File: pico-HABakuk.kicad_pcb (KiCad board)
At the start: 2 copper layers, 52 x 51 mm, 34 parts, among them J1 USB_B_Micro, J2 Conn_01x02, J3 Conn_02x18_Odd_Even, J4 Conn_02x18_Odd_Even, U1 NCP1117-3.3_SOT223, U2 W25Q128JVS, U3 RP2040, Y1 ABM8-272-T3

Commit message: First changes in the sch and pcb
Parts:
- removed J3, J4: Conn_02x18_Odd_Even, Connector_PinHeader_2.54mm:PinHeader_2x18_P2.54mm_Vertical
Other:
- board text added: "RP2040"
- board text added: "pico-HABakuk"
- board text removed: "Minimal Design Example REV2"
- board text removed: "Outer Row GND"
- board text removed: "Raspberry Pi RP2040"

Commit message: More work on schematics
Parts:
- removed H1, H2, H3, H4: MountingHole, MountingHole:MountingHole_2.7mm_M2.5
- removed R2: DNF, Resistor_SMD:R_0402_1005Metric
- added C18: 10u/4, Capacitor_SMD:C_0603_1608Metric, F.Cu at (137.7, 90.8)
- added C19: 10u/4, Capacitor_SMD:C_0603_1608Metric, F.Cu at (137.7, 93.3)
- added C20: 10u/4, Capacitor_SMD:C_0603_1608Metric, F.Cu at (137.7, 95.8)
- added C21: 1n, Capacitor_SMD:C_0603_1608Metric, F.Cu at (137.7, 98.3)
- added C22: 1u, Capacitor_SMD:C_0603_1608Metric, F.Cu at (141.7, 90.8)
- added C23: 1n, Capacitor_SMD:C_0603_1608Metric, F.Cu at (141.7, 93.3)
- added C24: 10u/10, Capacitor_SMD:C_0805_2012Metric, F.Cu at (149.9, 94.6)
- added D2: WS2812B-2020, LED_SMD:LED_WS2812B-2020_PLCC4_2.0x2.0mm, F.Cu at (154.1, 91.3)
- added J4: Ant-, Connector_PinHeader_2.54mm:PinHeader_1x01_P2.54mm_Vertical, F.Cu at (160.8, 109.6)
- added J5: Solar, Connector_PinSocket_2.54mm:PinSocket_1x02_P2.54mm_Vertical, F.Cu at (148.0, 101.9)
- added J7: Ultra_Cap, Connector_PinSocket_2.54mm:PinSocket_1x02_P2.54mm_Vertical, F.Cu at (152.6, 101.9)
- added JP1: Solar_voltage, Jumper:SolderJumper-2_P1.3mm_Bridged_RoundedPad1.0x1.5mm, F.Cu at (149.9, 91.3)
- added L1: 10u, Inductor_SMD:L_Taiyo-Yuden_MD-3030, F.Cu at (149.6, 115.4)
- added R10: 360k, Resistor_SMD:R_0603_1608Metric, F.Cu at (145.7, 95.8)
- added R11: 220k, Resistor_SMD:R_0603_1608Metric, F.Cu at (145.7, 98.3)
- added R6: 1k, Resistor_SMD:R_0603_1608Metric, F.Cu at (141.7, 95.8)
- added R7: 1k, Resistor_SMD:R_0603_1608Metric, F.Cu at (141.7, 98.3)
- added R8: 1k, Resistor_SMD:R_0603_1608Metric, F.Cu at (145.7, 90.8)
- added R9: 510m, Resistor_SMD:R_0603_1608Metric, F.Cu at (145.7, 93.3)
- added SW1: USB BOOT, Button_Switch_SMD:SW_SPST_Omron_B3FS-100xP, F.Cu at (138.7, 119.0)
- added SW2: RESET, Button_Switch_SMD:SW_SPST_Omron_B3FS-100xP, F.Cu at (138.9, 107.5)
- added TP1: +3V3, Connector_Pin:Pin_D1.1mm_L8.5mm_W2.5mm_FlatFork, F.Cu at (137.9, 83.1)
- added TP2: USB_D+, Connector_Pin:Pin_D1.1mm_L8.5mm_W2.5mm_FlatFork, F.Cu at (137.9, 87.4)
- added TP3: USB_D-, Connector_Pin:Pin_D1.1mm_L8.5mm_W2.5mm_FlatFork, F.Cu at (142.5, 83.1)
- added TP4: GND, Connector_Pin:Pin_D1.1mm_L8.5mm_W2.5mm_FlatFork, F.Cu at (142.5, 87.4)
- added TP5: USB_BOOT, Connector_Pin:Pin_D1.1mm_L8.5mm_W2.5mm_FlatFork, F.Cu at (147.0, 83.1)
- added TP6: Reset, Connector_Pin:Pin_D1.1mm_L8.5mm_W2.5mm_FlatFork, F.Cu at (147.0, 87.4)
- added TP7: SWCLK, Connector_Pin:Pin_D1.1mm_L8.5mm_W2.5mm_FlatFork, F.Cu at (151.6, 83.1)
- added TP8: SWD, Connector_Pin:Pin_D1.1mm_L8.5mm_W2.5mm_FlatFork, F.Cu at (151.6, 87.4)
- added U4: SPV1040T, Package_SO:TSSOP-8_4.4x3mm_P0.65mm, F.Cu at (150.1, 109.0)
- added U5: LM4040DBZ-3, Package_TO_SOT_SMD:SOT-23, F.Cu at (149.4, 126.1)
- C10: value 1u -> 2u2
- J2: value Conn_01x02 -> Ant+; footprint Connector_PinHeader_2.54mm:PinHeader_1x02_P2.54mm_Vertical -> Connector_PinHeader_2.54mm:PinHeader_1x01_P2.54mm_Vertical
- moved J2 74.0 mm to (160.8, 101.4), turned to 0 degrees
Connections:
- net /XIN renamed Net-(U3-XIN)
- net /XOUT renamed Net-(U3-XOUT)
- net VBUS renamed Net-(J1-VBUS)
- C10 pad 1: +3V3 -> Net-(U3-VREG_IN)
- J2 pad 1: /~{USB_BOOT} -> /GPIO6
- U3 pad 44: +3V3 -> Net-(U3-VREG_IN)
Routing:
- net +3V3: track 42.6 -> 40.2 mm
- net Net-(U3-VREG_IN): track 0.00 -> 2.44 mm

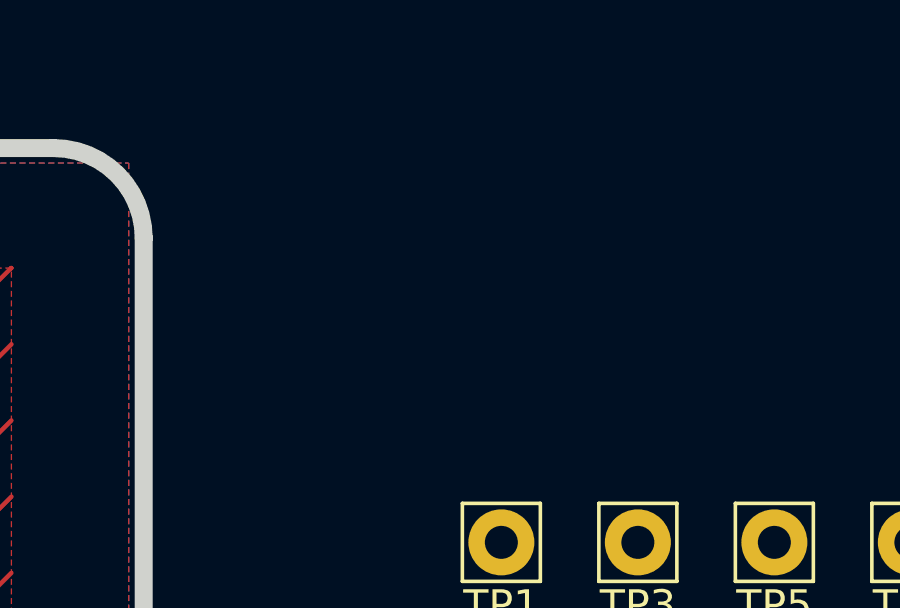
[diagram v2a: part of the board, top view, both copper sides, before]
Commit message: GPS module added to schematics
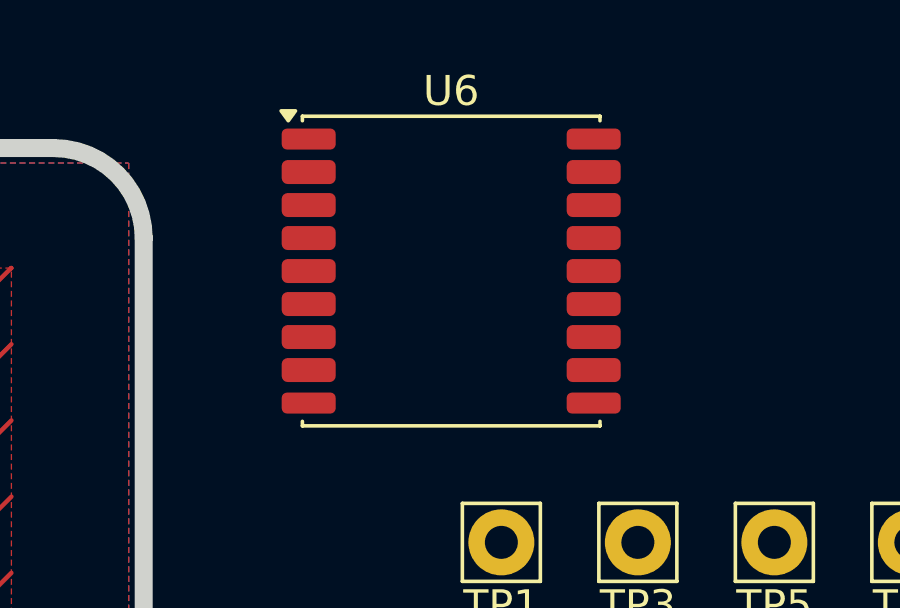
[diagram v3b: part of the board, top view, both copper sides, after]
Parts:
- added U6: MAX-8Q, RF_GPS:ublox_MAX, F.Cu at (136.2, 74.1)
- J7: value Ultra_Cap -> Super_Cap
